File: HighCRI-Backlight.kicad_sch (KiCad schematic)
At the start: 115 parts, among them J1 Conn_01x03, J2 Screw_Terminal_01x02, J3 Screw_Terminal_01x02, Q1 AOD4130, Q2 AOD4130, Q3 AOD4130, U1 L78L24_SO8, U2 LM324

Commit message: Basic PCB Layout
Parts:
- added H1, H2, H3, H4: MountingHole_Pad, MountingHole:MountingHole_3.2mm_M3_DIN965_Pad_TopBottom, symbol Mechanical:MountingHole_Pad
- J2, J3: URL (none) -> https://www.ebay.com/itm/192840344146?epid=8029762746&_trkp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
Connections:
- net GND: now also H1.1, H2.1, H3.1, H4.1
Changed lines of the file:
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@@
   (junction (at 168.91 153.67) (diameter 0) (color 0 0 0 0)
   )
+  (junction (at 39.37 116.84) (diameter 0) (color 0 0 0 0)
+  )
   (junction (at 209.55 147.32) (diameter 0) (color 0 0 0 0)
   )
   (junction (at 74.93 157.48) (diameter 0) (color 0 0 0 0)
   )
+  (junction (at 45.72 116.84) (diameter 0) (color 0 0 0 0)
+  )
   (junction (at 111.76 138.43) (diameter 0) (color 0 0 0 0)
   )
@@
   (junction (at 43.18 157.48) (diameter 0) (color 0 0 0 0)
   )
+  (junction (at 52.07 116.84) (diameter 0) (color 0 0 0 0)
+  )
   (junction (at 111.76 153.67) (diameter 0) (color 0 0 0 0)
   )
@@
     (stroke (width 0) (type default) (color 0 0 0 0))
   )
+  (wire (pts (xy 26.67 114.3) (xy 26.67 116.84))
+    (stroke (width 0) (type default) (color 0 0 0 0))
+  )
   (wire (pts (xy 64.77 87.63) (xy 59.69 87.63))
     (stroke (width 0) (type default) (color 0 0 0 0))
@@
     (stroke (width 0) (type default) (color 0 0 0 0))
   )
+  (wire (pts (xy 26.67 116.84) (xy 39.37 116.84))
+    (stroke (width 0) (type default) (color 0 0 0 0))
+  )
   (wire (pts (xy 34.29 53.34) (xy 31.75 53.34))
     (stroke (width 0) (type default) (color 0 0 0 0))
   )
+  (wire (pts (xy 52.07 116.84) (xy 45.72 116.84))
+    (stroke (width 0) (type default) (color 0 0 0 0))
+  )
   (wire (pts (xy 92.71 74.93) (xy 92.71 78.74))
     (stroke (width 0) (type default) (color 0 0 0 0))
@@
     (stroke (width 0) (type default) (color 0 0 0 0))
   )
+  (wire (pts (xy 52.07 116.84) (xy 64.77 116.84))
+    (stroke (width 0) (type default) (color 0 0 0 0))
+  )
   (wire (pts (xy 111.76 86.36) (xy 111.76 90.17))
     (stroke (width 0) (type default) (color 0 0 0 0))
@@
     (stroke (width 0) (type default) (color 0 0 0 0))
   )
+  (wire (pts (xy 52.07 114.3) (xy 52.07 116.84))
+    (stroke (width 0) (type default) (color 0 0 0 0))
+  )
   (wire (pts (xy 34.29 52.07) (xy 34.29 53.34))
     (stroke (width 0) (type default) (color 0 0 0 0))
@@
     (stroke (width 0) (type default) (color 0 0 0 0))
   )
+  (wire (pts (xy 64.77 114.3) (xy 64.77 116.84))
+    (stroke (width 0) (type default) (color 0 0 0 0))
+  )
   (wire (pts (xy 168.91 97.79) (xy 168.91 101.6))
     (stroke (width 0) (type default) (color 0 0 0 0))
@@
     (stroke (width 0) (type default) (color 0 0 0 0))
   )
+  (wire (pts (xy 39.37 116.84) (xy 39.37 114.3))
+    (stroke (width 0) (type default) (color 0 0 0 0))
+  )
   (wire (pts (xy 130.81 109.22) (xy 130.81 113.03))
     (stroke (width 0) (type default) (color 0 0 0 0))
@@
     (stroke (width 0) (type default) (color 0 0 0 0))
   )
+  (wire (pts (xy 45.72 116.84) (xy 39.37 116.84))
+    (stroke (width 0) (type default) (color 0 0 0 0))
+  )
   (wire (pts (xy 130.81 132.08) (xy 130.81 138.43))
     (stroke (width 0) (type default) (color 0 0 0 0))
@@
     (pin "2")
   )
+  (symbol (lib_id "power:GND") (at 45.72 116.84 0) (unit 1)
+    (in_bom yes) (on_board yes)
+    (property "Reference" "#PWR024" (id 0) (at 45.72 123.19 0)
+      (effects (font (size 1.27 1.27)) hide)
+    )
+    (property "Value" "GND" (id 1) (at 45.72 120.65 0))
+    (property "Footprint" "" (id 2) (at 45.72 116.84 0)
+      (effects (font (size 1.27 1.27)) hide)
+    )
+    (property "Datasheet" "" (id 3) (at 45.72 116.84 0)
+      (effects (font (size 1.27 1.27)) hide)
+    )
+    (pin "1")
+  )
   (symbol (lib_id "Device:LED") (at 207.01 128.27 90) (unit 1)
     (in_bom yes) (on_board yes) (fields_autoplaced)
@@
     (pin "2")
   )
+  (symbol (lib_id "Mechanical:MountingHole_Pad") (at 39.37 111.76 0) (unit 1)
+    (in_bom yes) (on_board yes) (fields_autoplaced)
+    (property "Reference" "H2" (id 0) (at 41.91 109.2199 0)
+      (effects (font (size 1.27 1.27)) (justify left))
+    )
+    (property "Value" "MountingHole_Pad" (id 1) (at 41.91 111.7599 0)
+      (effects (font (size 1.27 1.27)) (justify left))
+    )
+    (property "Footprint" "MountingHole:MountingHole_3.2mm_M3_DIN965_Pad_TopBottom" (id 2) (at 39.37 111.76 0)
+      (effects (font (size 1.27 1.27)) hide)
+    )
+    (property "Datasheet" "~" (id 3) (at 39.37 111.76 0)
+      (effects (font (size 1.27 1.27)) hide)
+    )
+    (pin "1")
+  )
   (symbol (lib_id "Device:LED") (at 224.79 48.26 90) (unit 1)
     (in_bom yes) (on_board yes) (fields_autoplaced)
@@
     (pin "2")
   )
+  (symbol (lib_id "Mechanical:MountingHole_Pad") (at 64.77 111.76 0) (unit 1)
+    (in_bom yes) (on_board yes) (fields_autoplaced)
+    (property "Reference" "H4" (id 0) (at 67.31 109.2199 0)
+      (effects (font (size 1.27 1.27)) (justify left))
+    )
+    (property "Value" "MountingHole_Pad" (id 1) (at 67.31 111.7599 0)
+      (effects (font (size 1.27 1.27)) (justify left))
+    )
+    (property "Footprint" "MountingHole:MountingHole_3.2mm_M3_DIN965_Pad_TopBottom" (id 2) (at 64.77 111.76 0)
+      (effects (font (size 1.27 1.27)) hide)
+    )
+    (property "Datasheet" "~" (id 3) (at 64.77 111.76 0)
+      (effects (font (size 1.27 1.27)) hide)
+    )
+    (pin "1")
+  )
   (symbol (lib_id "Device:C") (at 53.34 147.32 0) (unit 1)
     (in_bom yes) (on_board yes) (fields_autoplaced)
@@
     (pin "1")
   )
+  (symbol (lib_id "Mechanical:MountingHole_Pad") (at 52.07 111.76 0) (unit 1)
+    (in_bom yes) (on_board yes) (fields_autoplaced)
+    (property "Reference" "H3" (id 0) (at 54.61 109.2199 0)
+      (effects (font (size 1.27 1.27)) (justify left))
+    )
+    (property "Value" "MountingHole_Pad" (id 1) (at 54.61 111.7599 0)
+      (effects (font (size 1.27 1.27)) (justify left))
+    )
+    (property "Footprint" "MountingHole:MountingHole_3.2mm_M3_DIN965_Pad_TopBottom" (id 2) (at 52.07 111.76 0)
+      (effects (font (size 1.27 1.27)) hide)
+    )
+    (property "Datasheet" "~" (id 3) (at 52.07 111.76 0)
+      (effects (font (size 1.27 1.27)) hide)
+    )
+    (pin "1")
+  )
   (symbol (lib_id "Device:LED") (at 243.84 59.69 90) (unit 1)
     (in_bom yes) (on_board yes) (fields_autoplaced)
@@
       (effects (font (size 1.27 1.27)) hide)
     )
+    (property "URL" "https://www.ebay.com/itm/192840344146?epid=8029762746&_trkparms=ispr%3D1&hash=item2ce62e2252:g:AAEAAOSwyhBcddkx&amdata=enc%3AAQAGAAAA4GlQRaV0kVJ%2BfatZOiIvI7gK3jCY4e%2FgQQLNpiEjhFaS5wt6ACAGzfVbKZalcnf%2BYX%2FYSiu7kM1EHKzYB%2BCwUcN6FvfmgkV9%2BwhcBX9kZb2iHXEkM660zFg09pJ0lLRy9wkDAKMh2YVhgocE1Vc2wCZWaUbUQpQfm7y%2BEDr4qz8K%2BtV1zoigDT4n9M8C3Nn2XT22tIYjXSWXojX2qu0TTxSAmLNbx7dOM0fkCxxoXMOobFzlkODA%2BNjE9HPV35w%2BujSaQk%2B7Z5RmtYte8485yQoIIsVNSKLoozOnWVRj%2BvC%2F%7Ctkp%3ABFBMqMjFs_1f" (id 4) (at 29.21 24.13 90)
+      (effects (font (size 1.27 1.27)) hide)
+    )
     (pin "1")
     (pin "2")
@@
       (effects (font (size 1.27 1.27)) hide)
     )
+    (property "URL" "https://www.ebay.com/itm/192840344146?epid=8029762746&_trkparms=ispr%3D1&hash=item2ce62e2252:g:AAEAAOSwyhBcddkx&amdata=enc%3AAQAGAAAA4GlQRaV0kVJ%2BfatZOiIvI7gK3jCY4e%2FgQQLNpiEjhFaS5wt6ACAGzfVbKZalcnf%2BYX%2FYSiu7kM1EHKzYB%2BCwUcN6FvfmgkV9%2BwhcBX9kZb2iHXEkM660zFg09pJ0lLRy9wkDAKMh2YVhgocE1Vc2wCZWaUbUQpQfm7y%2BEDr4qz8K%2BtV1zoigDT4n9M8C3Nn2XT22tIYjXSWXojX2qu0TTxSAmLNbx7dOM0fkCxxoXMOobFzlkODA%2BNjE9HPV35w%2BujSaQk%2B7Z5RmtYte8485yQoIIsVNSKLoozOnWVRj%2BvC%2F%7Ctkp%3ABFBMqMjFs_1f" (id 4) (at 59.69 24.13 90)
+      (effects (font (size 1.27 1.27)) hide)
+    )
     (pin "1")
     (pin "2")
@@
     (pin "2")
   )
+  (symbol (lib_id "Mechanical:MountingHole_Pad") (at 26.67 111.76 0) (unit 1)
+    (in_bom yes) (on_board yes) (fields_autoplaced)
+    (property "Reference" "H1" (id 0) (at 29.21 109.2199 0)
+      (effects (font (size 1.27 1.27)) (justify left))
+    )
+    (property "Value" "MountingHole_Pad" (id 1) (at 29.21 111.7599 0)
+      (effects (font (size 1.27 1.27)) (justify left))
+    )
+    (property "Footprint" "MountingHole:MountingHole_3.2mm_M3_DIN965_Pad_TopBottom" (id 2) (at 26.67 111.76 0)
+      (effects (font (size 1.27 1.27)) hide)
+    )
+    (property "Datasheet" "~" (id 3) (at 26.67 111.76 0)
+      (effects (font (size 1.27 1.27)) hide)
+    )
+    (pin "1")
+  )
   (symbol (lib_id "Device:LED") (at 149.86 82.55 90) (unit 1)
     (in_bom yes) (on_board yes) (fields_autoplaced)
@@
       (reference "#PWR023") (unit 1) (value "+36V") (footprint "")
     )
+    (path "/03d630c9-f866-41f7-86da-ab7e8338bafc"
+      (reference "#PWR024") (unit 1) (value "GND") (footprint "")
+    )
     (path "/b329b040-9afa-4c31-95a5-a96ccf592fdd"
       (reference "C1") (unit 1) (value "100nF") (footprint "Capacitor_SMD:C_1206_3216Metric_Pad1.33x1.80mm_HandSolder")
@@
       (reference "D90") (unit 1) (value "3000k LED") (footprint "ClementsFootprints:LED_1212_3030METRIC_MP-3030")
     )
+    (path "/ecb6539c-5f0d-4aaf-b54b-85f80e2a3cce"
+      (reference "H1") (unit 1) (value "MountingHole_Pad") (footprint "MountingHole:MountingHole_3.2mm_M3_DIN965_Pad_TopBottom")
+    )
+    (path "/0d4412d9-d0cd-40f4-97c9-95716367ce87"
+      (reference "H2") (unit 1) (value "MountingHole_Pad") (footprint "MountingHole:MountingHole_3.2mm_M3_DIN965_Pad_TopBottom")
+    )
+    (path "/3e948e40-efd0-4e67-a761-03f2678fc2b0"
+      (reference "H3") (unit 1) (value "MountingHole_Pad") (footprint "MountingHole:MountingHole_3.2mm_M3_DIN965_Pad_TopBottom")
+    )
+    (path "/191384f1-6edc-4eb0-9874-01d20dacf24d"
+      (reference "H4") (unit 1) (value "MountingHole_Pad") (footprint "MountingHole:MountingHole_3.2mm_M3_DIN965_Pad_TopBottom")
+    )
     (path "/74e4259b-df22-4ea6-a8a3-5dbbff5336b6"

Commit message: Routing Seemingly Complete
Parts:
- R1: footprint Resistor_SMD:R_0603_1608Metric_Pad0.98x0.95mm_HandSolder -> Resistor_SMD:R_1206_3216Metric_Pad1.30x1.75mm_HandSolder
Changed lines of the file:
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@@
     (property "Reference" "R1" (id 0) (at 68.58 53.34 90))
     (property "Value" "0R" (id 1) (at 68.58 55.88 90))
-    (property "Footprint" "Resistor_SMD:R_0603_1608Metric_Pad0.98x0.95mm_HandSolder" (id 2) (at 68.58 58.42 0)
+    (property "Footprint" "Resistor_SMD:R_1206_3216Metric_Pad1.30x1.75mm_HandSolder" (id 2) (at 68.58 58.42 0)
       (effects (font (size 1.27 1.27)) hide)
     )
@@
     )
     (path "/d2949b6c-9d11-4fc2-ba23-9fd6d309e80a"
-      (reference "R1") (unit 1) (value "0R") (footprint "Resistor_SMD:R_0603_1608Metric_Pad0.98x0.95mm_HandSolder")
+      (reference "R1") (unit 1) (value "0R") (footprint "Resistor_SMD:R_1206_3216Metric_Pad1.30x1.75mm_HandSolder")
     )
     (path "/6b1b6f5c-54ce-4ce9-9d20-270dfdfda1c7"

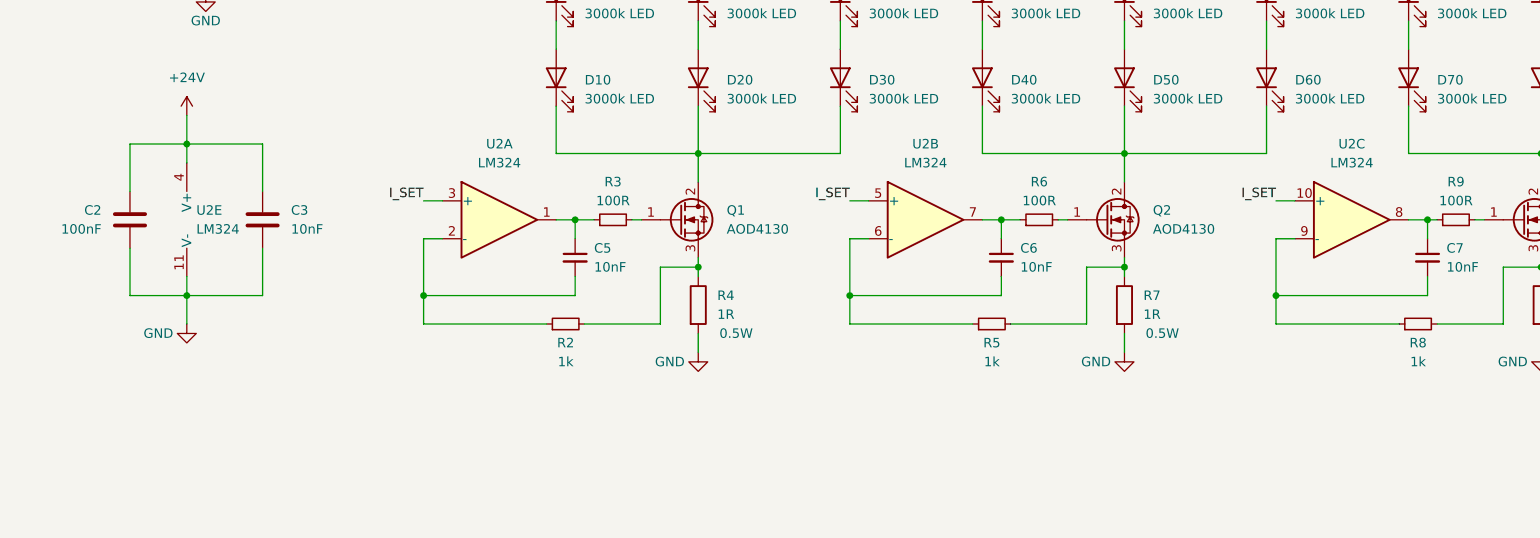
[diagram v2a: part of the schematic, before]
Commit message: Finished Single Sided Design
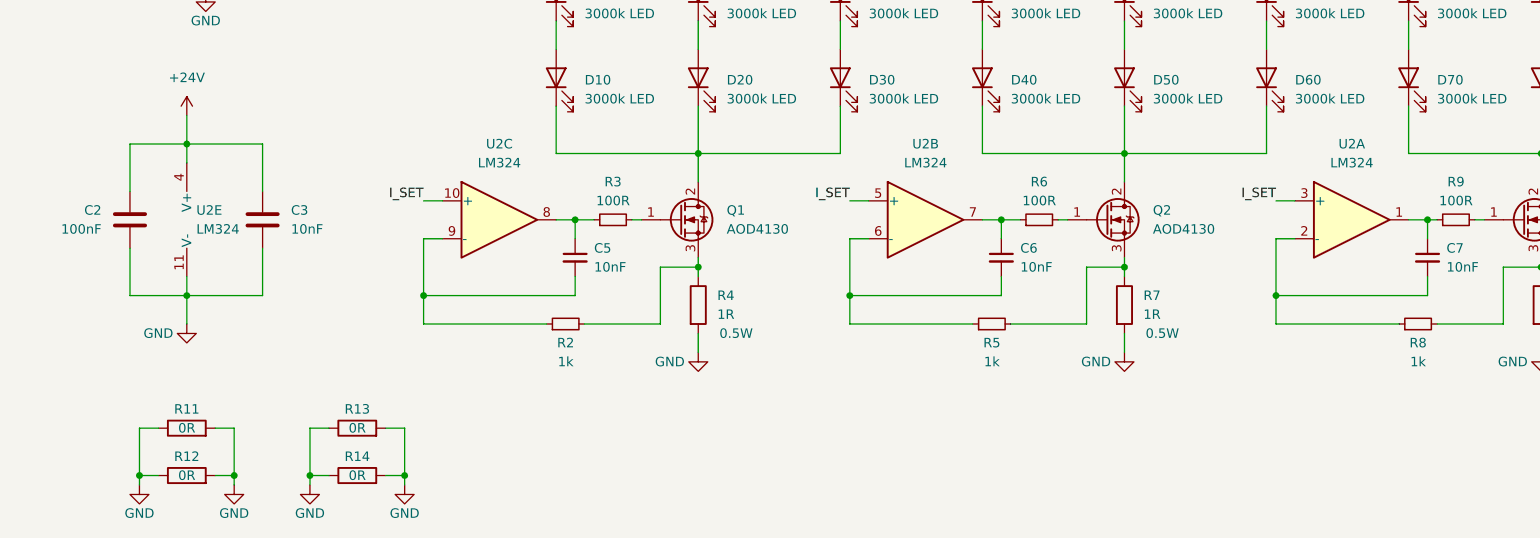
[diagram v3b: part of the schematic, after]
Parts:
- added R11, R12, R13, R14: 0R, Resistor_SMD:R_1206_3216Metric_Pad1.30x1.75mm_HandSolder, symbol Device:R
- C5, C6, C7: footprint Resistor_SMD:R_0805_2012Metric_Pad1.20x1.40mm_HandSolder -> Capacitor_SMD:C_1206_3216Metric_Pad1.33x1.80mm_HandSolder
- R10, R4, R7: footprint Resistor_SMD:R_1210_3225Metric_Pad1.30x2.65mm_HandSolder -> Resistor_SMD:R_1206_3216Metric_Pad1.30x1.75mm_HandSolder
- R2, R3, R5, R6, R8, R9: footprint Resistor_SMD:R_0603_1608Metric_Pad0.98x0.95mm_HandSolder -> Resistor_SMD:R_1206_3216Metric_Pad1.30x1.75mm_HandSolder
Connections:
- net GND: now also R11.1, R11.2, R12.1, R12.2, R13.1, R13.2, R14.1, R14.2
- net at C5.1, R3.1: now also U2.8; no longer U2.1
- net at C5.2, R2.1: now also U2.9 (-); no longer U2.2 (-)
- net at C7.2, R8.1: now also U2.2 (-); no longer U2.9 (-)
- net at C7.1, R9.1: now also U2.1; no longer U2.8
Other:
- moved on the sheet: U2A, U2C
